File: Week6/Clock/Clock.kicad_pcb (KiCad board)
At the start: 2 copper layers, 140 x 90 mm, 50 parts, among them J1 Power_inlet_vertical, J2 Conn_01x06, SW1 RotaryEncoder_Switch, SW2 Omron_B3F_SPST, U2 ATmega328-PU, U3 L7805_TO92, U4 DS1307_DIP-8, U5 MAX7219, U6 MAX7219, Y1 Crystal 16MHZ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

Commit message: Week 7 Update !
It's great :smile:
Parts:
- added C12: C_0805_1uf, footprints:C_0805_2012Metric, B.Cu at (213.1, 118.0)
- added DO_TP1: TestPoint, footprints:TestPoint_THTPad_D2.0mm_Drill1.0mm, F.Cu at (163.6, 141.1)
- added RX_TP1: TestPoint, footprints:TestPoint_THTPad_D2.0mm_Drill1.0mm, F.Cu at (190.0, 112.3)
- added TP_GND1: TestPoint, footprints:TestPoint_THTPad_D2.0mm_Drill1.0mm, F.Cu at (201.3, 141.6)
- added TX_TP1: TestPoint, footprints:TestPoint_THTPad_D2.0mm_Drill1.0mm, F.Cu at (190.1, 107.5)
- renumbered TP2 to A_TP1, TP3 to B_TP1, TP4 to VBAT_TP1, TP1 to VCC_TP1
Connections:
- U5 pad 24: unconnected-(U5-Pad24) -> Net-(U5-Pad24)
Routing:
- net Net-(U5-Pad24): track 0.00 -> 42.6 mm, vias 0 -> 3
- net GND: track 46.6 -> 53.6 mm
- net ROT ENC SWITCH: track 71.6 -> 75.7 mm
- net TXD: track 16.9 -> 20.9 mm
- net RXD: track 22.6 -> 26.1 mm
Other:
- board text added: "Bryan's Beauty"

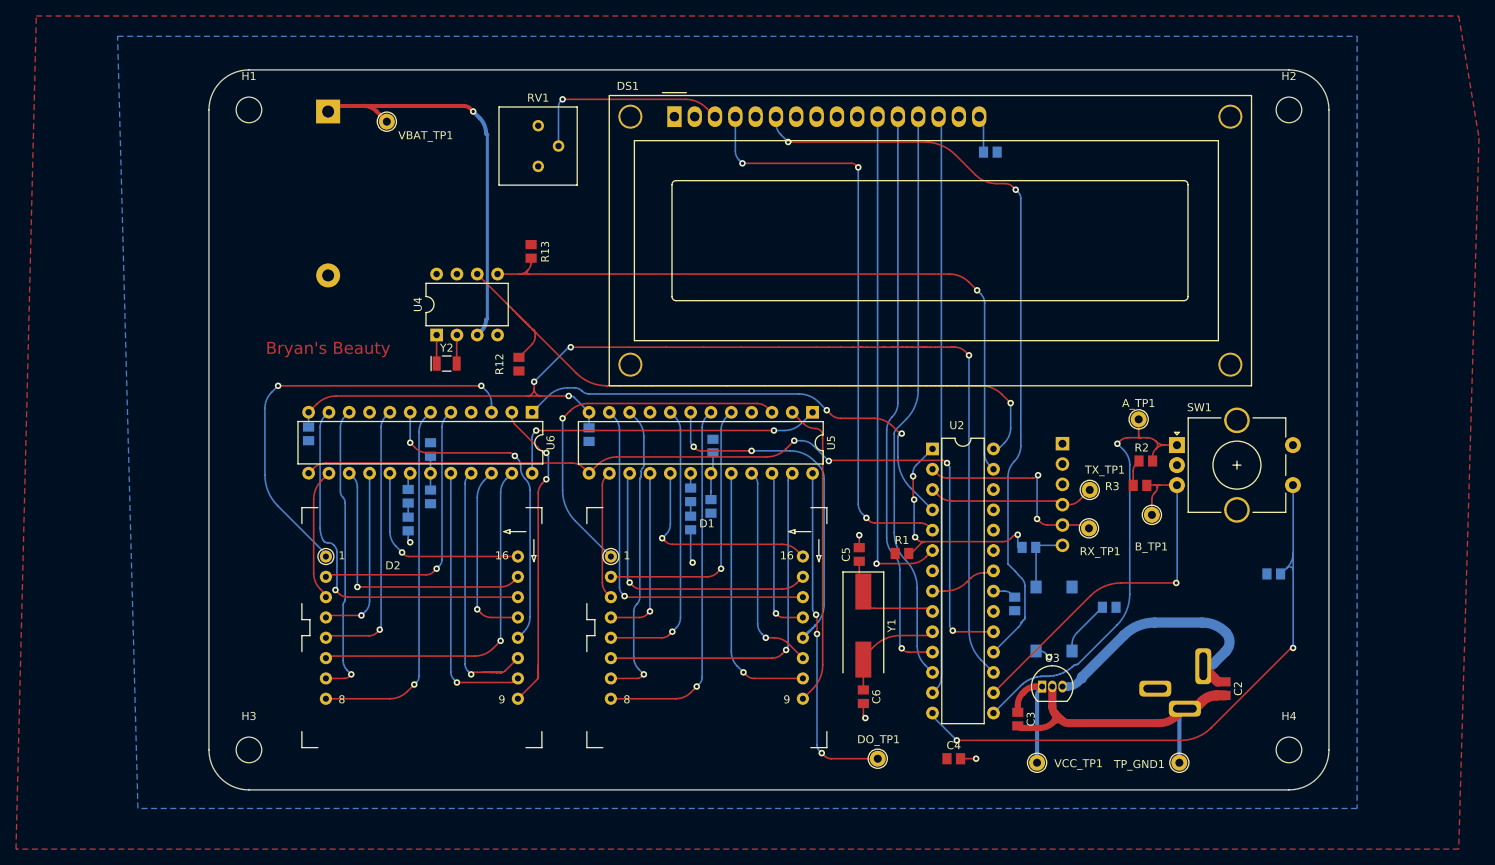
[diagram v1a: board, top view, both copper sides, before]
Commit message: Fixed PCB & Gerber
No more backsided SMT
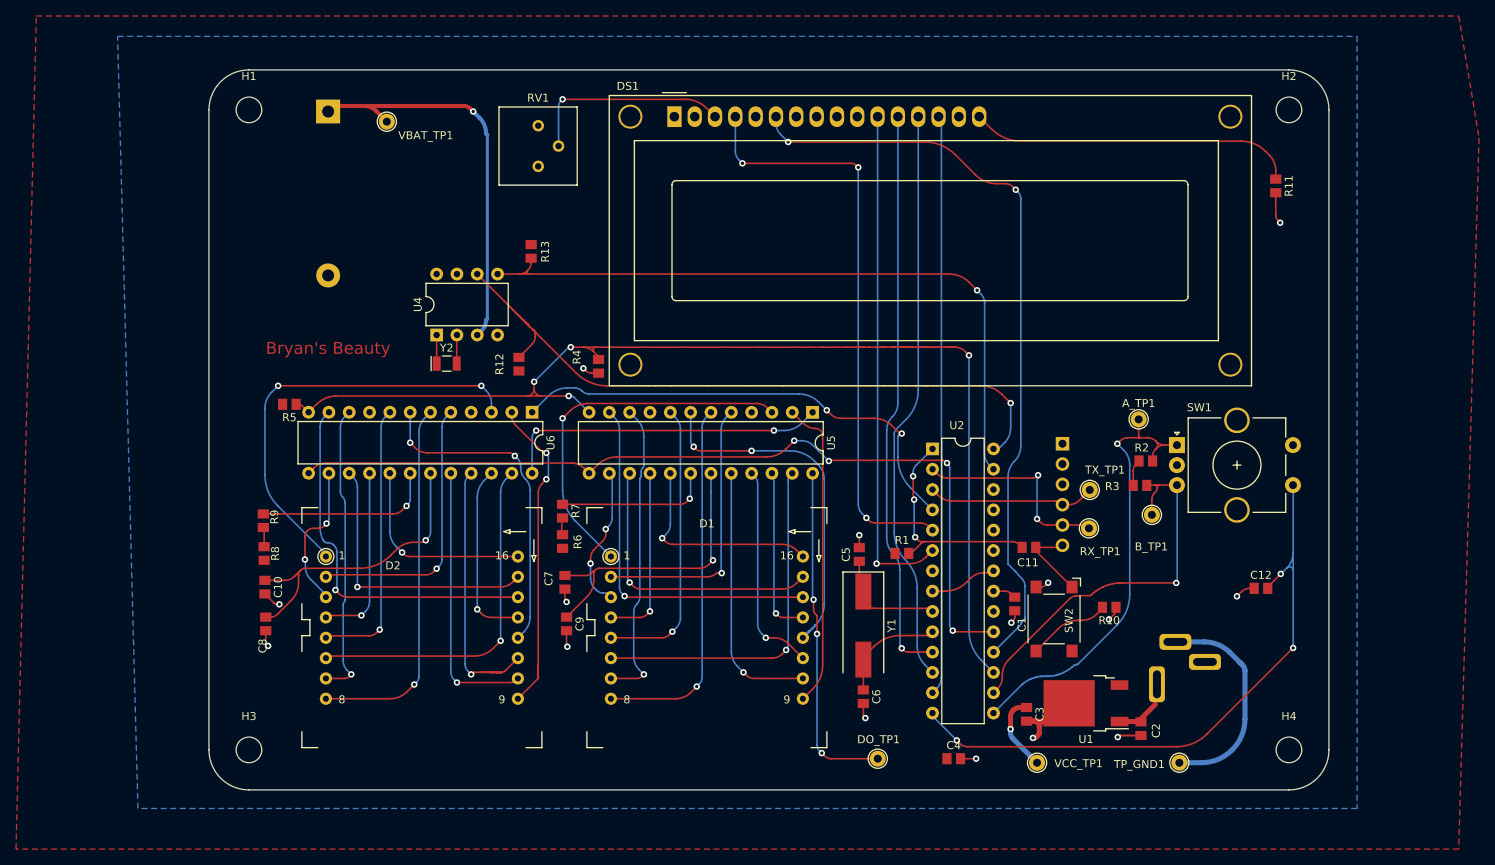
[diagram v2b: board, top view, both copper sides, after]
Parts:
- removed U3: L7805_TO92, footprints:TO-92_Inline
- added U1: L7805, footprints:TO-252-2, F.Cu at (189.6, 134.2)
- C1, C10, C11, C12, C7, C8, C9, R10, R11, R4, R5, R6, R7, R8, R9, SW2: moved to F.Cu
- moved R11 35.9 mm to (213.3, 69.5), turned to -90 degrees
- moved C9 28.8 mm to (124.7, 124.2), turned to -90 degrees
- moved C10 26.9 mm to (87.0, 119.7), turned to -90 degrees
- moved C8 26.0 mm to (87.1, 124.2)
- moved C7 20.6 mm to (124.5, 119.0)
- moved R8 18.4 mm to (86.9, 115.5)
- moved R9 18.4 mm to (86.8, 111.3)
- moved R6 16.2 mm to (124.2, 114.0)
- moved R7 16.1 mm to (124.2, 110.2)
- moved C2 11.6 mm to (196.5, 137.3)
- moved R4 8.62 mm to (128.7, 92.0)
- moved R5 4.41 mm to (90.0, 96.8), turned to 180 degrees
- moved J1 2.56 mm to (202.0, 131.8), turned to 0 degrees
- moved C12 2.41 mm to (211.5, 119.8)
- moved C3 1.25 mm to (182.2, 135.6)
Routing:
- net VCC: track 36.0 -> 89.3 mm
- net Net-(DS1-Pad16): track 4.62 -> 42.1 mm
- net Net-(C2-Pad1): track 33.5 -> 5.37 mm
- net GND: track 53.6 -> 74.7 mm, vias 3 -> 14
- net Net-(R9-Pad2): track 2.12 -> 22.9 mm, vias 0 -> 1
- net Net-(R7-Pad2): track 1.85 -> 19.4 mm, vias 0 -> 1
- net Net-(R10-Pad2): track 6.93 -> 10.3 mm
- net ROT ENC SWITCH: track 75.7 -> 78.7 mm, vias 2 -> 3
- net Net-(D1-Pad3): track 16.1 -> 18.2 mm, vias 0 -> 2
- net Net-(D2-Pad3): track 16.4 -> 18.2 mm, vias 0 -> 2
- net ~{RESET BTN}: track 8.38 -> 10.1 mm
- net unconnected-(SW2-Pad3): track 0.00 -> 1.69 mm, vias 0 -> 1
- net ~{RST}: track 30.2 -> 28.6 mm, vias 4 -> 3
- net DATA MAX: track 141.1 -> 142.4 mm
- net ROT ENC B OUT: track 48.9 -> 50.0 mm
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
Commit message: Fixed weeks
Week 7 will now hold all future updates to the PCB ! (Including future weeks)
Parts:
- moved R5 1.50 mm to (89.4, 98.2), turned to -90 degrees
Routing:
- net DATA MAX: track 142.4 -> 144.4 mm
- net GND: track 74.7 -> 76.7 mm, vias 14 -> 15
- net unconnected-(SW2-Pad3): track 1.69 -> 0.00 mm, vias 1 -> 0
- net Net-(DS1-Pad16): track 42.1 -> 41.0 mm
- net Net-(R9-Pad2): track 22.9 -> 22.4 mm

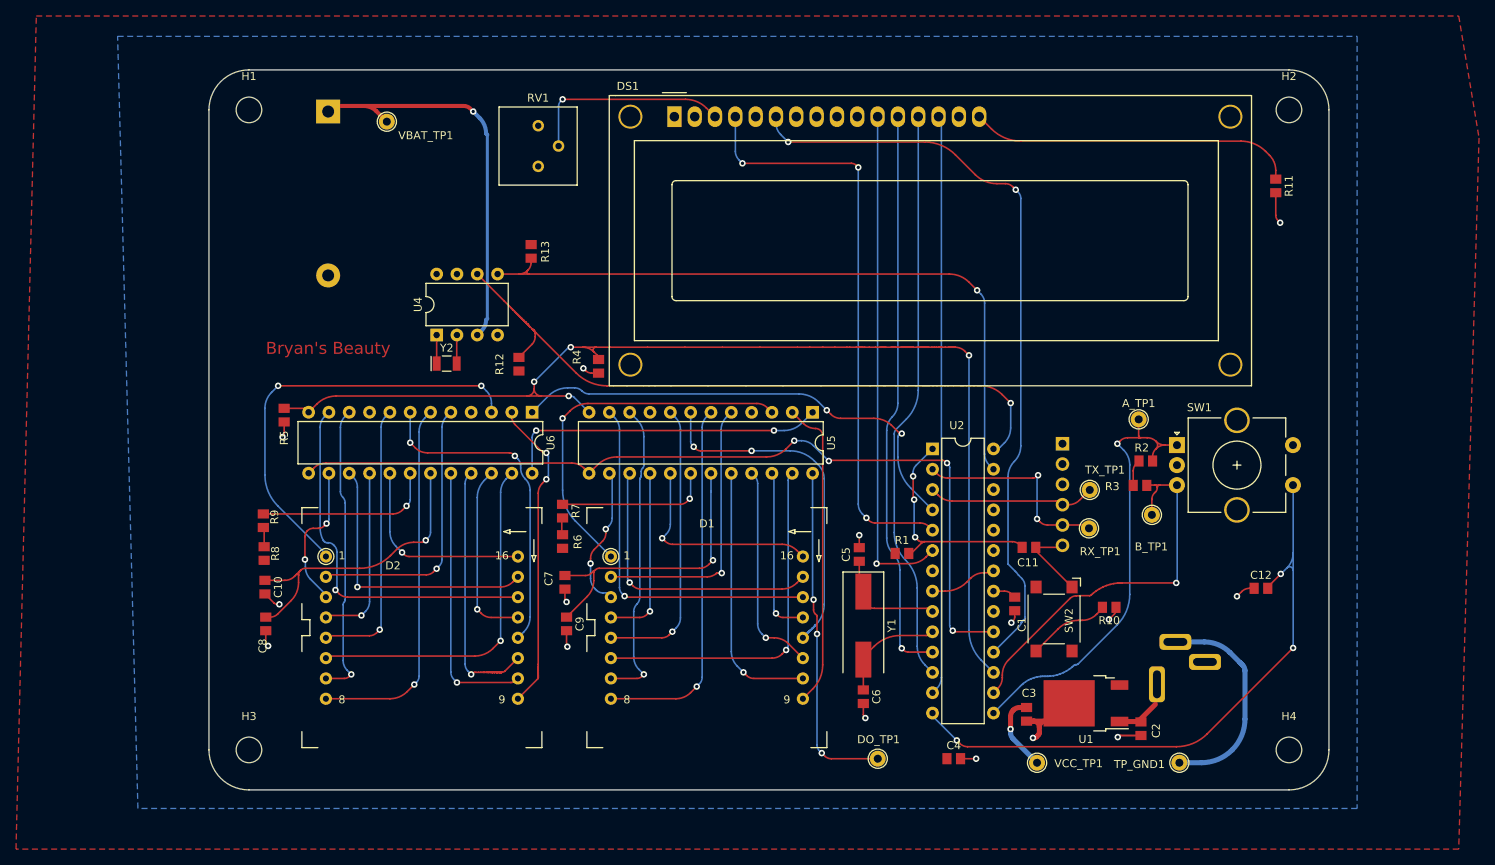
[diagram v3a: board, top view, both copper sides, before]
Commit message: Applied 12/12 rules
Fix gerbers as well !
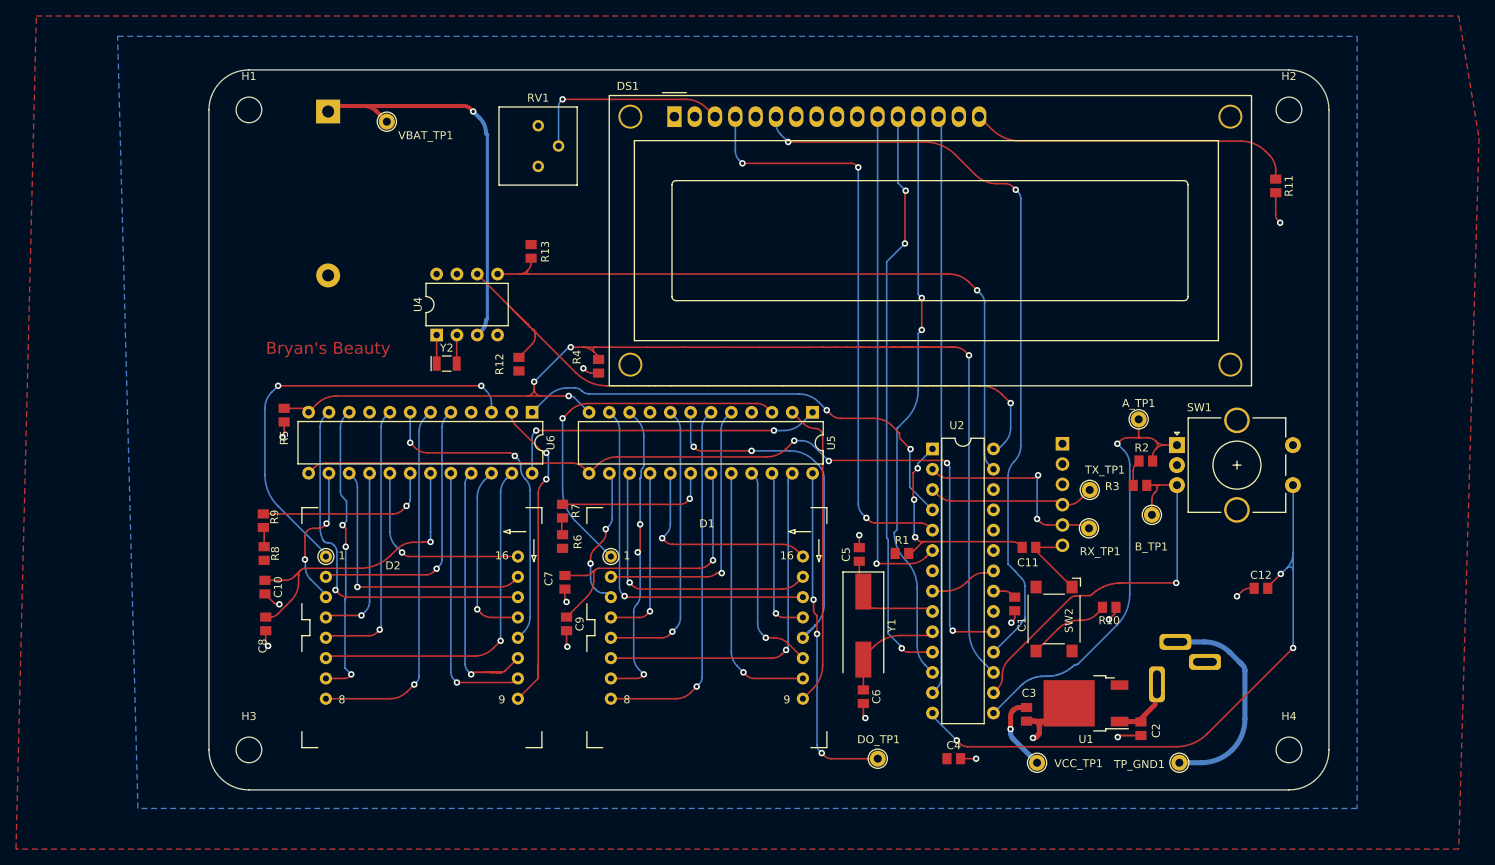
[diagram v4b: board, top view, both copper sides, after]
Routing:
- net LCD D5: track 71.3 -> 72.6 mm, vias 1 -> 3
- net Net-(D1-Pad7): track 38.4 -> 39.1 mm, vias 1 -> 3
- net LCD D6: track 71.8 -> 72.5 mm, vias 0 -> 2
- net Net-(D2-Pad7): track 37.0 -> 37.6 mm, vias 1 -> 3
- net VCC: track 89.0 -> 89.5 mm

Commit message: Uploaded Student Designs :)
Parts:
- removed the G*** at (140.8, 72.9)
- added C13: C_0805_0.1uf, footprints:C_0805_2012Metric, F.Cu at (180.8, 122.2)
- added D3: LED_0805, footprints:LED_0805_2012Metric, F.Cu at (199.9, 121.3)
- added G***: LOGO, Logo:abc, F.Cu at (95.6, 72.4)
- added G***: LOGO, Logo:ASCast, F.Cu at (214.6, 95.7)
- added G***: LOGO, Logo:Dare Greatly, F.Cu at (212.9, 85.0)
- added G***: LOGO, Logo:PS, B.Cu at (132.3, 79.6)
- added G***: LOGO, Logo:NBA, B.Cu at (151.1, 80.5)
- added G***: LOGO, Logo:Star, B.Cu at (177.2, 74.4)
- added R14: R_0805_1K, footprints:R_0805_2012Metric, F.Cu at (194.4, 126.7)
- C1: value 10uf -> C_0805_0.1uf
- C7, C8: value C_0805_1uf -> C_0805_10uf
- R10, R2, R3: value R_0805_200 -> R_0805_10K
- R12, R13: value R_0805_2.2K -> R_0805_4.7K
- R9: value R_0805_4.7K -> R_0805_10K
- moved R9 125.9 mm to (211.8, 126.2), turned to 180 degrees
- moved C1 4.68 mm to (181.8, 117.2), turned to 0 degrees
- moved C11 1.08 mm to (182.5, 113.6)
- moved C8 0.27 mm to (87.2, 124.5)
- moved R12 0.26 mm to (118.6, 92.0)
- moved R13 0.24 mm to (120.2, 77.5)
- moved R10 0.24 mm to (192.3, 122.1), turned to 0 degrees
- moved R2 0.21 mm to (196.2, 107.1)
- moved C7 0.15 mm to (124.5, 119.2)
- moved R3 0.13 mm to (197.0, 103.8), turned to 0 degrees
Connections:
- R10 pad 1: GND -> Net-(SW2-Pad4)
- R10 pad 2: Net-(R10-Pad2) -> GND
- R3 pad 1: ROT ENC A OUT -> VCC
- R3 pad 2: VCC -> ROT ENC A OUT
- R8 pad 2: Net-(R8-Pad2) -> Net-(U6-Pad18)
- R9 pad 1: Net-(R8-Pad2) -> ROT ENC SWITCH
- R9 pad 2: Net-(R9-Pad2) -> VCC
- SW2 pad 4: Net-(R10-Pad2) -> Net-(SW2-Pad4)
- U6 pad 18: Net-(R9-Pad2) -> Net-(U6-Pad18)
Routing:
- net Net-(U6-Pad18): track 0.00 -> 26.3 mm, vias 0 -> 1
- net Net-(R9-Pad2): track 22.4 -> 0.00 mm, vias 1 -> 0
- net SCK: track 109.0 -> 126.5 mm, vias 4 -> 6
- net Net-(SW2-Pad4): track 0.00 -> 10.3 mm
- net Net-(R10-Pad2): track 10.3 -> 0.00 mm
- net Net-(D3-Pad2): track 0.00 -> 9.22 mm
- net Net-(U2-Pad21): track 2.91 -> 6.52 mm
- net GND: track 76.7 -> 80.1 mm, vias 15 -> 17
- net VCC: track 89.5 -> 86.2 mm
- net ROT ENC SWITCH: track 78.7 -> 81.9 mm
- net Net-(R8-Pad2): track 2.43 -> 0.00 mm
